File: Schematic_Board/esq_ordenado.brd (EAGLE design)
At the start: 75.7 x 71.5 mm, 47 parts, among them IC1 LM1117IMPX-3.3, Q1 SMD-TRANSISTORS-NPN-25V-500MW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, Q2 SMD-TRANSISTORS-NPN-25V-500MW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, U1 ESP-32S, U2 CP2102-GM, U3 TPD2S017DBVR, U4 Value, U5 TMP275AIDR

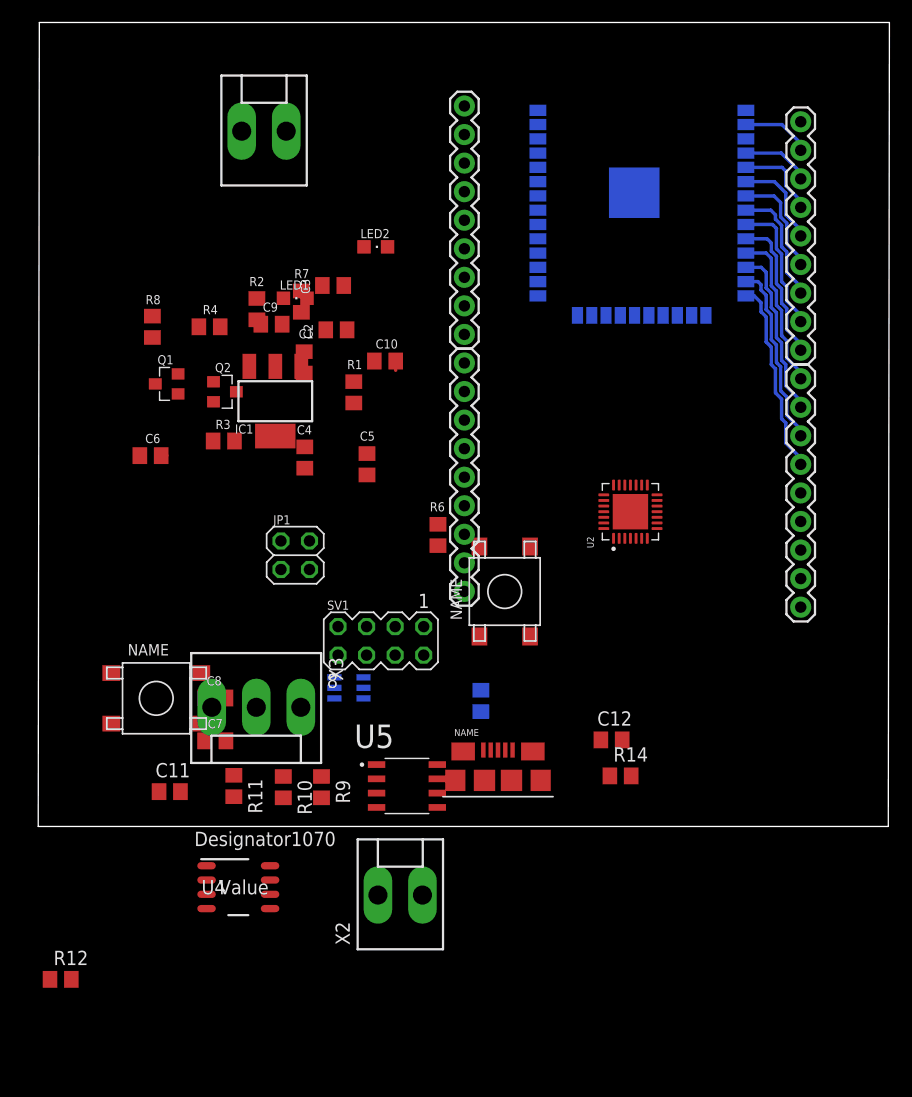
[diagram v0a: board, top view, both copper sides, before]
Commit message: Nuevos switch, option1 D+ D-
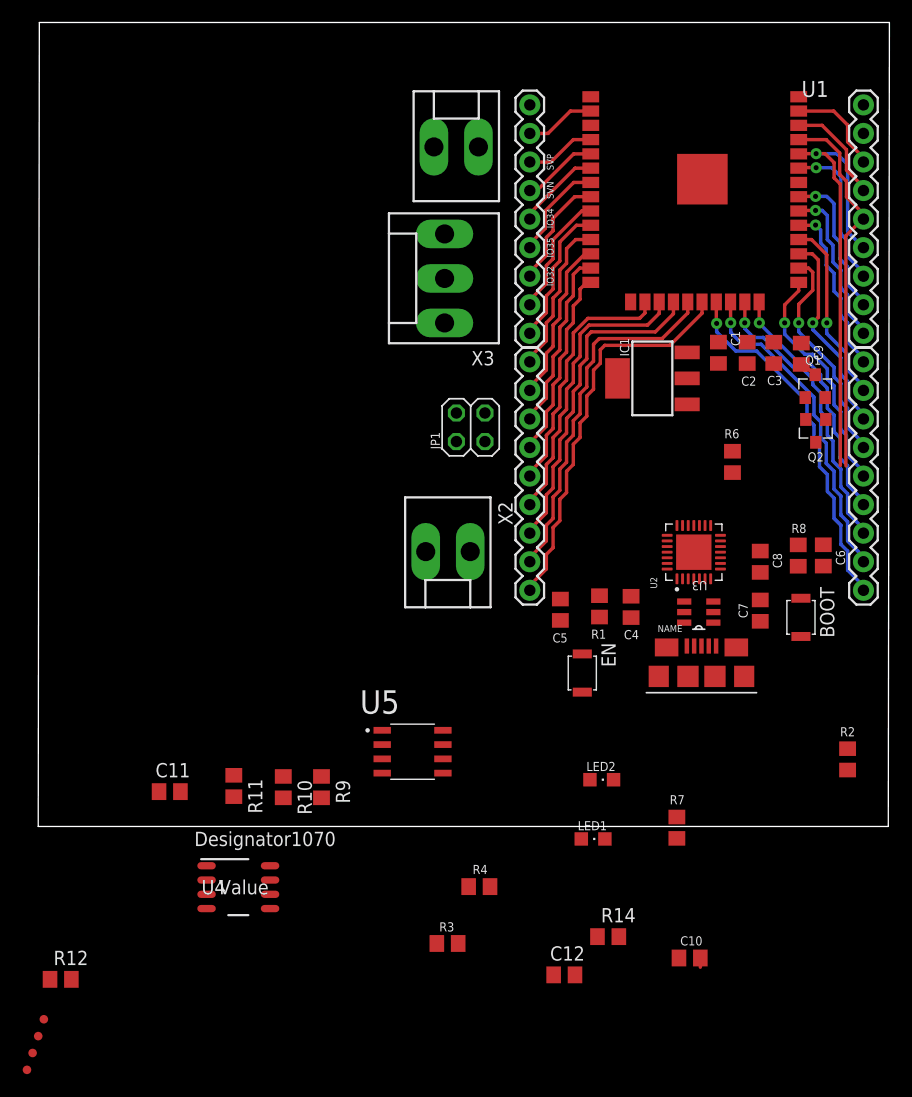
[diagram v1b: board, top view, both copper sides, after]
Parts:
- removed R5: 4.7K, resistor:R0805
- removed SV1: (no value), con-lstb:MA04-2
- removed S_IO0, U$2: SWITCH_OMRON_B3FS-1012P, switch_B3FS-1012P:B3FS-1012P
- added BOOT, EN: B3U-1000P, Switch:B3U-1000P
- added TP1, TP2, TP3, TP4: TEST-POINT3, SparkFun-Connectors:PAD.03X.03
- moved R2 66.1 mm to (72.0, 5.97)
- moved R8 60.9 mm to (67.6, 24.1)
- moved C6 60.5 mm to (69.8, 24.1), turned to 90 degrees
- moved C10 59.6 mm to (58.0, -11.7)
- moved Q1 57.7 mm to (69.1, 39.2), turned to 0 degrees
- moved R7 57.5 mm to (56.8, -0.11)
- moved R4 55.3 mm to (39.2, -5.35)
- moved LED1 54.9 mm to (49.4, -1.11)
- moved Q2 52.7 mm to (69.2, 35.2), turned to 180 degrees
- moved LED2 51.5 mm to (50.1, 4.16)
- moved C8 50.0 mm to (64.2, 23.6), turned to 90 degrees
- moved C7 49.8 mm to (64.2, 19.2), turned to 270 degrees
- moved R3 48.9 mm to (36.4, -10.4)
- moved C9 47.2 mm to (67.9, 42.0), turned to 90 degrees
- moved X3 41.7 mm to (36.1, 48.8), turned to 90 degrees
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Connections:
- removed net D+IN: SV1.6, U3.1
- removed net D-IN: SV1.8, U3.6
- removed net N$5: R5.2, U2.9
- net 3.3V: no longer R5.1
- net D+: now also TP1.P$1, U3.1; no longer SV1.1, SV1.5
- net D+_OUT: now also TP3.P$1; no longer SV1.2
- net D-: now also TP2.P$1, U3.6; no longer SV1.3, SV1.7
- net D-_OUT: now also TP4.P$1; no longer SV1.4
- net ENABLE: now also EN.1; no longer U$2.P1, U$2.P2
- net GND: now also BOOT.2, EN.2; no longer S_IO0.P3, S_IO0.P4, U$2.P3, U$2.P4
- net IO0: now also BOOT.1; no longer S_IO0.P1, S_IO0.P2
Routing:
- net RXD_ESP: track 0.00 -> 41.9 mm, vias 0 -> 1
- net CLK: track 0.00 -> 35.4 mm
- net TXD_ESP: track 0.00 -> 33.5 mm
- net CMD: track 0.00 -> 32.2 mm
- net SD0: track 0.00 -> 32.2 mm, vias 0 -> 1
- net SD3: track 0.00 -> 29.2 mm
- net SD1: track 0.00 -> 29.0 mm, vias 0 -> 1
- net IO15: track 0.00 -> 25.9 mm, vias 0 -> 1
- net SD2: track 0.00 -> 25.8 mm
- net IO13: track 0.00 -> 22.4 mm
- net IO2: track 0.00 -> 22.4 mm, vias 0 -> 1
- net IO0: track 0.88 -> 21.1 mm, vias 0 -> 1
- net IO4: track 0.00 -> 19.9 mm, vias 0 -> 1
- net IO16: track 0.00 -> 18.2 mm, vias 0 -> 1
- net IO17: track 0.00 -> 16.5 mm, vias 0 -> 1
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
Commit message: Version final-revision nicolas
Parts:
- removed X1, X2: (no value), con-molex:KK-156-2
- removed X3: (no value), con-molex:KK-156-3
- added C13, C14: 0.1uF, resistor:C0805
- added J3: (no value), SparkFun-Connectors:1X01
- added X4, X5: (no value), con-ptr500:AK500/2
- added X6: (no value), con-ptr500:AK500/3
- moved C10 72.9 mm to (10.8, 43.9)
- moved R7 66.9 mm to (6.41, 43.9), turned to 180 degrees
- moved LED2 57.5 mm to (4.43, 39.1)
- moved TP3 47.0 mm to (36.2, 9.15), flipped to the bottom
- moved TP1 46.3 mm to (36.2, 10.2), flipped to the bottom
- moved C9 45.8 mm to (27.9, 19.8), turned to 270 degrees
- moved C3 45.7 mm to (25.5, 19.8), turned to 270 degrees
- moved TP4 42.6 mm to (28.5, 9.15), flipped to the bottom
- moved C2 39.7 mm to (30.4, 19.6), turned to 270 degrees
- moved TP2 39.2 mm to (28.5, 10.2), flipped to the bottom
- moved C8 38.7 mm to (27.6, 10.8)
- moved R6 38.1 mm to (28.0, 14.8), flipped to the bottom, turned to 90 degrees
- moved C7 37.3 mm to (28.8, 7.57), turned to 180 degrees
- moved R3 37.1 mm to (31.7, 26.4), turned to 270 degrees
- moved R2 37.0 mm to (37.7, 19.8)
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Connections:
- net ENABLE: now also J3.1
- net GND: now also C13.2, C14.2, X4.2, X5.1, X6.2; no longer U$1.P4, X1.1, X2.2, X3.2
- net IO13: now also U4.4
- net IO4: no longer U4.4
- net V+: now also C13.1, X6.3; no longer X3.1
- net V-: now also C14.1, X6.1; no longer X3.3
- net VCC: now also X4.1; no longer X1.2
- net VRELE: now also X5.2; no longer X2.1
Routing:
- net 3.3V: track 6.24 -> 132.3 mm, vias 0 -> 2
- net VIN: track 0.00 -> 78.9 mm, vias 0 -> 1
- net VUSB: track 0.00 -> 69.9 mm, vias 0 -> 2
- net ENABLE: track 0.00 -> 69.1 mm, vias 0 -> 3
- net IO15: track 25.9 -> 64.0 mm
- net SD1: track 29.0 -> 65.2 mm
- net IO0: track 21.1 -> 49.8 mm, vias 1 -> 3
- net N$7: track 0.00 -> 21.0 mm
- net V+: track 0.00 -> 20.0 mm
- net DTR_CP: track 0.32 -> 20.2 mm, vias 0 -> 1
- net RTS_CP: track 0.00 -> 16.9 mm, vias 0 -> 1
- net VCC: track 0.82 -> 14.7 mm
- net VRELE: track 0.00 -> 13.1 mm
- net IO13: track 22.4 -> 34.6 mm, vias 0 -> 1
- net V-: track 0.00 -> 11.9 mm
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- added copper zone on layer 16, net 3.3V
- added copper zone on layer 1, net GND
- added copper zone on layer 16, net V+
- added copper zone on layer 16, net V-
- added copper zone on layer 16, net VCC
- added copper zone on layer 16, net VIN
- added copper zone on layer 16, net VRELE
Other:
- board size 75.7 x 71.5 mm -> 49.3 x 54 mm
- board text added: "EN"
- board text added: "NILM_UIS J. Nicolas Riaño T. Edwin Paez G."
- board text added: "V+"
- board text added: "V-"
- board text added: "VRELE"
- board text removed: "NILM_UIS"

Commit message: Correc Borneras - revision nicolas
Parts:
- removed X4, X5: (no value), con-ptr500:AK500/2
- removed X6: (no value), con-ptr500:AK500/3
- added U$2, U$3: PT2,5/2-5,0, con_phoenix:PT2,5/2-5,0
- added U$4: PT2,5/3-5,0, con_phoenix:PT2,5/3-5,0
- moved C13 5.34 mm to (1.40, 16.2), turned to 270 degrees
- moved R7 4.95 mm to (5.69, 39.0), turned to 270 degrees
- moved R12 2.60 mm to (11.5, 14.9)
- moved U4 1.90 mm to (6.50, 16.3)
- moved LED2 1.40 mm to (3.04, 39.2), turned to 0 degrees
- moved C10 1.07 mm to (11.6, 44.5), flipped to the bottom, turned to 90 degrees
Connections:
- net GND: now also U$2.PT1, U$3.PT2, U$4.PT2; no longer X4.2, X5.1, X6.2
- net V+: now also U$4.PT1; no longer X6.3
- net V-: now also U$4.PT3; no longer X6.1
- net VCC: now also U$2.PT2; no longer X4.1
- net VRELE: now also U$3.PT1; no longer X5.2
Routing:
- net GND: track 6.91 -> 10.6 mm
- net V+: track 20.0 -> 23.6 mm
- net N$6: track 5.72 -> 2.70 mm
- net IO13: track 34.6 -> 32.8 mm
- net VCC: track 14.7 -> 13.5 mm
- net VRELE: track 13.1 -> 14.1 mm
- net VIN: track 78.9 -> 78.3 mm
- net N$8: track 9.22 -> 8.62 mm
- added copper zone on layer 1, net V+
- added copper zone on layer 1, net V-
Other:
- board text added: "VIN"
- board text added: "VUSB"

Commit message: centrar PCB - revision nicolas
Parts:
- moved Q1 1.41 mm to (36.0, 28.2)
- moved R14 1.41 mm to (41.7, 4.20)
- moved C11 1.41 mm to (26.6, 10.7)
- moved EN 1.41 mm to (21.4, 15.1)
- moved R9 1.41 mm to (21.8, 10.7)
- moved U5 1.41 mm to (22.3, 4.75)
- moved C2 1.41 mm to (31.8, 19.4)
- moved C3 1.41 mm to (26.9, 19.6)
- moved C4 1.41 mm to (26.0, 15.7)
- moved C8 1.41 mm to (29.0, 10.7)
- moved R1 1.41 mm to (24.5, 19.5)
- moved R3 1.41 mm to (33.1, 26.2)
- moved J5 1.41 mm to (15.8, 51.7)
- moved J6 1.41 mm to (15.8, 28.8)
- moved R12 1.41 mm to (12.9, 14.7)
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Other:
- board size 49.3 x 54 mm -> 47.9 x 54 mm

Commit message: DRC Y ERC CHECK - revision nicolas
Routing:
- net GND: track 10.6 -> 35.5 mm, vias 2 -> 3
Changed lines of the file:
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@@
 <wire x1="29.5" y1="13.4" x2="25.1" y2="13.4" width="0.3048" layer="1"/>
 <wire x1="21.8" y1="11.65" x2="22" y2="11.65" width="0.3048" layer="1"/>
-<wire x1="26.3" y1="9.75" x2="26.6" y2="9.75" width="0.3048" layer="1"/>
 <wire x1="25" y1="6.655" x2="25.955" y2="6.655" width="0.3048" layer="1"/>
 <wire x1="25.955" y1="6.655" x2="26.7" y2="7.4" width="0.3048" layer="1"/>
@@
 <wire x1="13" y1="45.3" x2="10.5" y2="47.8" width="0.1524" layer="16"/>
 <wire x1="10.5" y1="47.8" x2="10.3" y2="47.8" width="0.1524" layer="16"/>
-<wire x1="29.03" y1="11.6" x2="29.36" y2="13.68" width="0" layer="19" extent="1-16"/>
+<wire x1="28.2" y1="2.1" x2="24.6" y2="2.1" width="0.3048" layer="16"/>
+<wire x1="29.36" y1="11.68" x2="27.76" y2="10.08" width="0.3048" layer="16"/>
+<wire x1="29.36" y1="11.68" x2="29.36" y2="13.68" width="0.3048" layer="16"/>
+<via x="28.2" y="2.1" extent="1-16" drill="0.45" diameter="1"/>
+<wire x1="19.9" y1="6.8" x2="19.9" y2="8.8" width="0.3048" layer="16"/>
+<wire x1="19.9" y1="8.8" x2="21.18" y2="10.08" width="0.3048" layer="16"/>
+<wire x1="21.18" y1="10.08" x2="27.76" y2="10.08" width="0.3048" layer="16"/>
+<wire x1="24.6" y1="2.1" x2="19.9" y2="6.8" width="0.3048" layer="16"/>
 </signal>
 <signal name="ENABLE" class="1">
@@
 <wire x1="30.4" y1="17.2" x2="22.9" y2="17.2" width="0.3048" layer="16"/>
 <via x="22.9" y="17.2" extent="1-16" drill="0.45" diameter="1"/>
-<wire x1="22" y1="18.83" x2="21.7" y2="18.83" width="0.3048" layer="1"/>
 <wire x1="21.7" y1="18.83" x2="21.45" y2="18.83" width="0.3048" layer="1"/>
 <wire x1="24.53" y1="18.53" x2="24.53" y2="16.17" width="0.3048" layer="1"/>
@@
 <contactref element="U1" pad="7"/>
 <contactref element="J5" pad="6"/>
-<wire x1="21.25" y1="44.79" x2="21.15" y2="44.69" width="0.3048" layer="1"/>
 <wire x1="15.83" y1="39.33" x2="15.83" y2="38.99" width="0.3048" layer="1"/>
 <wire x1="17.2" y1="40.7" x2="15.83" y2="39.33" width="0.3048" layer="1"/>
@@
 <contactref element="J1" pad="6"/>
 <contactref element="U2" pad="26"/>
-<wire x1="39.75" y1="47.33" x2="39.77" y2="47.35" width="0.3048" layer="1"/>
 <wire x1="39.75" y1="47.33" x2="41.07341875" y2="47.33" width="0.3048" layer="1"/>
 <wire x1="45.36" y1="39.54" x2="45.36" y2="38.99" width="0.3048" layer="1"/>
@@
 <contactref element="U1" pad="33"/>
 <contactref element="J1" pad="7"/>
-<wire x1="39.75" y1="46.06" x2="39.8" y2="46.11" width="0.3048" layer="1"/>
 <wire x1="39.75" y1="46.06" x2="40.8968375" y2="46.06" width="0.3048" layer="1"/>
 <wire x1="40.8968375" y1="46.06" x2="42.75" y2="44.2068375" width="0.3048" layer="1"/>
@@
 <wire x1="45.36" y1="18.67" x2="44.43" y2="19.6" width="0.3048" layer="16"/>
 <via x="40.9" y="17.1" extent="1-16" drill="0.45" diameter="1"/>
-<wire x1="41.1" y1="15.50781875" x2="41.36" y2="15.34" width="0.3048" layer="1"/>
 <wire x1="44.43" y1="19.6" x2="40.5" y2="19.6" width="0.3048" layer="16"/>
 <wire x1="40.5" y1="19.6" x2="40.1" y2="19.2" width="0.3048" layer="16"/>
 <wire x1="40.1" y1="19.2" x2="40.1" y2="17.9" width="0.3048" layer="16"/>
 <wire x1="40.1" y1="17.9" x2="40.9" y2="17.1" width="0.3048" layer="16"/>
-<wire x1="40.9" y1="17.1" x2="41.1" y2="16.9" width="0.3048" layer="1"/>
-<wire x1="41.1" y1="16.9" x2="41.1" y2="15.50781875" width="0.3048" layer="1"/>
-<wire x1="41.36" y1="15.34" x2="40.46" y2="15.34" width="0.3048" layer="1"/>
-<wire x1="40.46" y1="15.34" x2="40.1" y2="14.98" width="0.3048" layer="1"/>
+<wire x1="40.9" y1="17.1" x2="41.3" y2="16.7" width="0.3048" layer="1"/>
+<wire x1="40.1" y1="14.98" x2="40.46" y2="15.34" width="0.3048" layer="1"/>
 <wire x1="40.1" y1="14.98" x2="40.1" y2="11.15" width="0.3048" layer="1"/>
 <wire x1="40.1" y1="11.15" x2="39.1" y2="10.15" width="0.3048" layer="1"/>
-<wire x1="41.36" y1="15.34" x2="41.23761875" y2="15.46238125" width="0.3048" layer="1"/>
-<wire x1="41.243334375" y1="15.51" x2="41.23761875" y2="15.46238125" width="0.3048" layer="1"/>
 <wire x1="40.9" y1="17.1" x2="39.8" y2="17.1" width="0.3048" layer="1"/>
 <wire x1="38.29" y1="15.59" x2="38.29" y2="15.35" width="0.3048" layer="1"/>
 <wire x1="39.8" y1="17.1" x2="38.29" y2="15.59" width="0.3048" layer="1"/>
+<wire x1="40.46" y1="15.34" x2="41.36" y2="15.34" width="0.3048" layer="1"/>
+<wire x1="41.3" y1="15.4" x2="41.36" y2="15.34" width="0.3048" layer="1"/>
+<wire x1="41.3" y1="16.7" x2="41.3" y2="15.4" width="0.3048" layer="1"/>
 </signal>
 <signal name="IO2" class="1">
@@
 <wire x1="44" y1="17.1" x2="44" y2="15.4" width="0.3048" layer="1"/>
 <wire x1="44" y1="15.4" x2="45.36" y2="14.04" width="0.3048" layer="1"/>
-<wire x1="24.2" y1="9.75" x2="24.05" y2="9.75" width="0.3048" layer="1"/>
 <via x="24.1" y="8" extent="1-16" drill="0.45" diameter="1"/>
 <wire x1="45.36" y1="13.59" x2="45.36" y2="13.16" width="0.3048" layer="16"/>
@@
 <contactref element="LED1" pad="A"/>
 <contactref element="R2" pad="2"/>
-<wire x1="39.1" y1="20.52" x2="39.12" y2="20.54" width="0.3048" layer="1"/>
+<wire x1="36.02" y1="20.52" x2="35.99" y2="20.49" width="0.3048" layer="1"/>
 <wire x1="39.1" y1="20.52" x2="36.02" y2="20.52" width="0.3048" layer="1"/>
-<wire x1="36.02" y1="20.52" x2="35.99" y2="20.49" width="0.3048" layer="1"/>
 </signal>
 <signal name="N$3">
@@
 <wire x1="8.995925" y1="40.3" x2="8.115925" y2="39.76" width="0.3048" layer="1"/>
 <wire x1="8.115925" y1="39.76" x2="7.09" y2="39.76" width="0.3048" layer="1"/>
-<polygon width="0.1524" layer="16" thermals="no">
-<vertex x="9.1" y="41"/>
-<vertex x="9.7" y="41.6"/>
-<vertex x="10.6" y="41.6"/>
-<vertex x="11.4" y="40.8"/>
-<vertex x="11.4" y="37.5"/>
-<vertex x="12.4" y="36.5"/>
-<vertex x="13.3" y="36.5"/>
-<vertex x="14.5" y="35.3"/>
+<polygon width="0.127" layer="16" isolate="0.3048" thermals="no">
+<vertex x="9.2" y="41"/>
+<vertex x="9.8" y="41.6"/>
+<vertex x="11" y="41.6"/>
+<vertex x="11.5" y="41.1"/>
+<vertex x="11.5" y="37.2"/>
+<vertex x="12.2" y="36.5"/>
+<vertex x="13" y="36.5"/>
+<vertex x="14.5" y="35"/>
 <vertex x="14.5" y="20.4"/>
-<vertex x="13.8" y="19.7"/>
-<vertex x="13" y="19.7"/>
-<vertex x="12.5" y="19.2"/>
-<vertex x="12.5" y="18.3"/>
-<vertex x="13" y="17.8"/>
-<vertex x="13.8" y="17.8"/>
-<vertex x="14.5" y="17.1"/>
-<vertex x="14.5" y="7.9"/>
-<vertex x="15.1" y="7.3"/>
-<vertex x="16.7" y="7.3"/>
-<vertex x="17.2" y="7.8"/>
-<vertex x="17.2" y="21.2"/>
-<vertex x="20.1" y="24.1"/>
-<vertex x="22" y="24.1"/>
-<vertex x="22.3" y="23.8"/>
-<vertex x="22.3" y="23.4"/>
-<vertex x="20.5" y="21.6"/>
-<vertex x="20.5" y="6.9"/>
-<vertex x="18.2" y="4.6"/>
-<vertex x="15.3" y="4.6"/>
-<vertex x="9.9" y="10"/>
-<vertex x="9.9" y="20.4"/>
-<vertex x="11.4" y="21.9"/>
-<vertex x="11.4" y="34.9"/>
-<vertex x="9.1" y="37.2"/>
+<vertex x="13.7" y="19.6"/>
+<vertex x="13" y="19.6"/>
+<vertex x="12.5" y="19.1"/>
+<vertex x="12.5" y="18.4"/>
+<vertex x="13" y="17.9"/>
+<vertex x="13.9" y="17.9"/>
+<vertex x="14.6" y="17.2"/>
+<vertex x="14.6" y="7.9"/>
+<vertex x="15.3" y="7.2"/>
+<vertex x="16.5" y="7.2"/>
+<vertex x="17.2" y="7.9"/>
+<vertex x="17.2" y="23.2"/>
+<vertex x="18.3" y="24.3"/>
+<vertex x="21.7" y="24.3"/>
+<vertex x="22.2" y="23.8"/>
+<vertex x="22.2" y="23.1"/>
+<vertex x="20.7" y="21.6"/>
+<vertex x="20.7" y="10.4"/>
+<vertex x="19.4" y="9.1"/>
+<vertex x="19.4" y="5.3"/>
+<vertex x="18.3" y="4.2"/>
+<vertex x="15" y="4.2"/>
+<vertex x="13.7" y="5.5"/>
+<vertex x="13.7" y="7.6"/>
+<vertex x="9.6" y="11.7"/>
+<vertex x="9.6" y="20.2"/>
+<vertex x="11.3" y="21.9"/>
+<vertex x="11.3" y="34.9"/>
+<vertex x="9.2" y="37"/>
 </polygon>
 </signal>
